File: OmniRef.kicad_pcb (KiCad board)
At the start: 2 copper layers, 79.5 x 50.5 mm, 105 parts, among them J1 4mm Banana Jack Pair, J2 4mm Banana Jack Pair, Q1 PMBT3906, SW1 SW_DPDT_x2, U1 REFERENCE IC, U2 LP2951, U3 REFERENCE IC, U4 AP3015

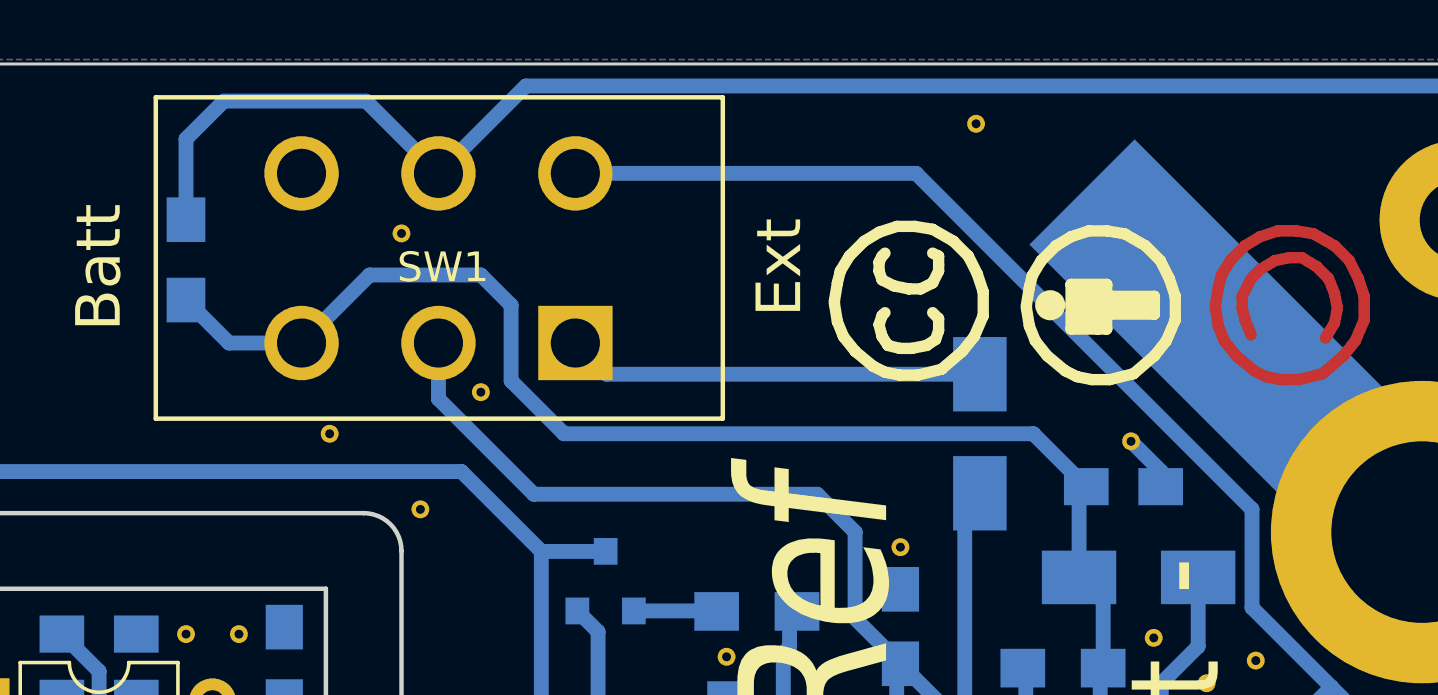
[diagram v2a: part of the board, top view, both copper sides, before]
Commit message: Selected resistors for switching regulator.  Fixed SW1 wiring.
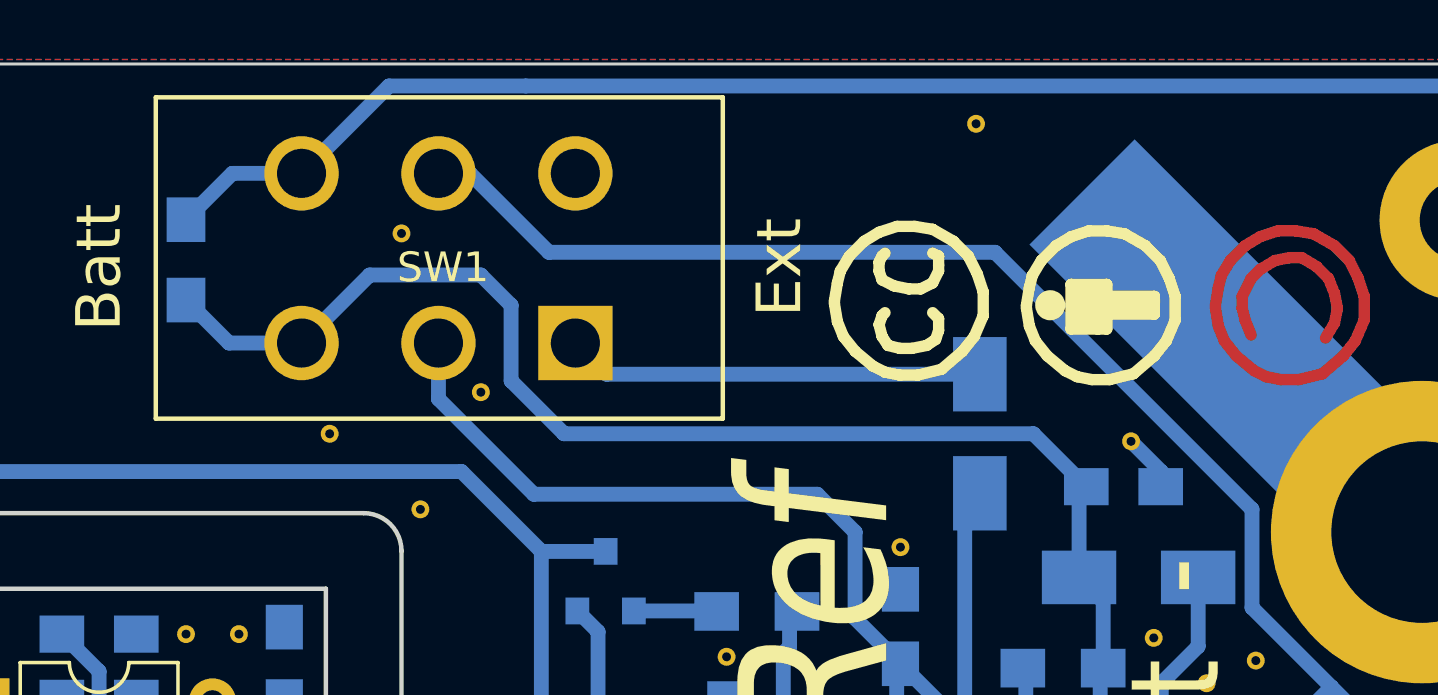
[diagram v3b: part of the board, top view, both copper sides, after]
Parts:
- R12: value R -> 1M
- R13: value R -> 82K
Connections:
- BT1 pad 0: GND -> (no net)
- SW1 pad 4: Net-(C11-Pad1) -> Net-(SW1-Pad4)
- SW1 pad 5: Net-(BT1-Pad1) -> Net-(C11-Pad1)
- SW1 pad 6: (no net) -> Net-(BT1-Pad1)
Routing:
- net Net-(C11-Pad1): track 53.1 -> 57.7 mm
- net Net-(BT1-Pad1): track 140.1 -> 136.5 mm
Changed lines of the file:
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@@
 (kicad_pcb (version 4) (host pcbnew 4.0.5)
   (general
-    (links 152)
+    (links 148)
     (no_connects 0)
-    (area 104.242399 57.785799 184.047601 108.584201)
+    (area 104.344999 57.884999 183.945001 108.485001)
     (thickness 1.6)
     (drawings 38)
-    (tracks 235)
+    (tracks 236)
     (zones 0)
     (modules 105)
-    (nets 26)
+    (nets 27)
   )
   (page A4)
@@
   (net 24 "Net-(C12-Pad2)")
   (net 25 "Net-(D8-Pad2)")
+  (net 26 "Net-(SW1-Pad4)")
   (net_class Default "This is the default net class."
     (clearance 0.2)
@@
     (add_net "Net-(Q1-Pad1)")
     (add_net "Net-(R2-Pad1)")
+    (add_net "Net-(SW1-Pad4)")
     (add_net "Net-(U2-Pad2)")
     (add_net "Net-(U2-Pad6)")
@@
     )
     (pad 0 thru_hole circle (at 8.89 -3.81) (size 2 2) (drill 1.5) (layers *.Cu)
-      (net 2 GND) (zone_connect 2))
+      (zone_connect 2))
     (pad 0 thru_hole circle (at 5.08 -3.81) (size 2 2) (drill 1.5) (layers *.Cu)
-      (net 2 GND) (zone_connect 2))
+      (zone_connect 2))
     (pad 0 thru_hole circle (at 8.89 0) (size 2 2) (drill 1.5) (layers *.Cu)
-      (net 2 GND) (zone_connect 2))
+      (zone_connect 2))
     (pad 2 smd oval (at 0 -3.81) (size 5.08 2.54) (layers B.Cu B.Mask)
       (net 2 GND))
@@
       (net 22 "Net-(BT1-Pad1)"))
     (pad 0 thru_hole circle (at 5.08 0) (size 2 2) (drill 1.5) (layers *.Cu)
-      (net 2 GND) (zone_connect 2))
+      (zone_connect 2))
   )
   (module _NTSFootprints:Via_Tented_0.3mm (layer F.Cu)
@@
       (net 17 BAT+))
     (pad 4 thru_hole circle (at 0 5.7 180) (size 2.5 2.5) (drill 1.65) (layers *.Cu *.Mask)
-      (net 23 "Net-(C11-Pad1)"))
+      (net 26 "Net-(SW1-Pad4)"))
     (pad 5 thru_hole circle (at 4.6 5.7 180) (size 2.5 2.5) (drill 1.65) (layers *.Cu *.Mask)
+      (net 23 "Net-(C11-Pad1)"))
+    (pad 6 thru_hole circle (at 9.2 5.7 180) (size 2.5 2.5) (drill 1.65) (layers *.Cu *.Mask)
       (net 22 "Net-(BT1-Pad1)"))
-    (pad 6 thru_hole circle (at 9.2 5.7 180) (size 2.5 2.5) (drill 1.65) (layers *.Cu *.Mask))
     (model ${KISYS3DMOD}/Buttons_Switches_THT.3dshapes/SW_CuK_JS202011CQN_DPDT_Straight.wrl
       (at (xyz 0 0 0))
@@
       (effects (font (size 1 1) (thickness 0.15)) (justify mirror))
     )
-    (fp_text value R (at 0 -1.75 180) (layer B.Fab)
+    (fp_text value 1M (at 0 -1.75 180) (layer B.Fab)
       (effects (font (size 1 1) (thickness 0.15)) (justify mirror))
     )
@@
       (effects (font (size 1 1) (thickness 0.15)) (justify mirror))
     )
-    (fp_text value R (at 0 -1.75 270) (layer B.Fab)
+    (fp_text value 82K (at 0 -1.75 270) (layer B.Fab)
       (effects (font (size 1 1) (thickness 0.15)) (justify mirror))
     )
@@
   (segment (start 155.913 77.513) (end 155.702 77.724) (width 0.5) (layer B.Cu) (net 14))
   (segment (start 148.336 70.358) (end 164.104 70.358) (width 0.5) (layer B.Cu) (net 17))
-  (segment (start 139.517 67.31) (end 141.803 65.024) (width 0.5) (layer B.Cu) (net 17))
   (segment (start 148.336 70.358) (end 146.558 68.58) (width 0.5) (layer B.Cu) (net 17))
   (segment (start 146.558 68.58) (end 146.558 66.04) (width 0.5) (layer B.Cu) (net 17))
   (segment (start 146.558 66.04) (end 145.542 65.024) (width 0.5) (layer B.Cu) (net 17))
-  (segment (start 145.542 65.024) (end 141.803 65.024) (width 0.5) (layer B.Cu) (net 17))
   (segment (start 164.104 70.358) (end 165.882 72.136) (width 0.5) (layer B.Cu) (net 17))
   (segment (start 165.64 75.184) (end 165.64 72.378) (width 0.5) (layer B.Cu) (net 17))
@@
   (segment (start 166.35 80.264) (end 166.35 78.332) (width 0.5) (layer B.Cu) (net 17))
   (segment (start 166.35 78.332) (end 166.45 78.232) (width 0.5) (layer B.Cu) (net 17))
-  (segment (start 139.517 67.31) (end 137.08 67.31) (width 0.5) (layer B.Cu) (net 17))
   (segment (start 137.08 67.31) (end 135.636 65.866) (width 0.5) (layer B.Cu) (net 17))
+  (segment (start 145.542 65.024) (end 141.803 65.024) (width 0.5) (layer B.Cu) (net 17))
+  (segment (start 139.517 67.31) (end 141.803 65.024) (width 0.5) (layer B.Cu) (net 17))
+  (segment (start 139.517 67.31) (end 137.08 67.31) (width 0.5) (layer B.Cu) (net 17))
   (segment (start 162.306 68.358) (end 149.765 68.358) (width 0.5) (layer B.Cu) (net 18))
   (segment (start 149.765 68.358) (end 148.717 67.31) (width 0.5) (layer B.Cu) (net 18))
@@
   (segment (start 152.94 94.71) (end 153.67 93.98) (width 0.5) (layer B.Cu) (net 21))
   (segment (start 149.32 95.885) (end 152.94 95.885) (width 0.5) (layer B.Cu) (net 21))
-  (segment (start 144.117 67.31) (end 144.117 69.187) (width 0.5) (layer B.Cu) (net 21))
-  (segment (start 144.117 69.187) (end 147.32 72.39) (width 0.5) (layer B.Cu) (net 21))
-  (segment (start 147.32 72.39) (end 156.845 72.39) (width 0.5) (layer B.Cu) (net 21))
-  (segment (start 156.845 72.39) (end 158.115 73.66) (width 0.5) (layer B.Cu) (net 21))
-  (segment (start 158.115 73.66) (end 158.115 76.561) (width 0.5) (layer B.Cu) (net 21))
   (segment (start 158.115 76.561) (end 159.639 78.085) (width 0.5) (layer B.Cu) (net 21))
   (segment (start 159.639 78.085) (end 159.365 78.085) (width 0.5) (layer B.Cu) (net 21))
   (segment (start 159.512 80.485) (end 159.512 78.212) (width 0.5) (layer B.Cu) (net 21))
+  (segment (start 158.115 73.66) (end 158.115 76.561) (width 0.5) (layer B.Cu) (net 21))
+  (segment (start 156.845 72.39) (end 158.115 73.66) (width 0.5) (layer B.Cu) (net 21))
+  (segment (start 144.117 67.31) (end 144.117 69.187) (width 0.5) (layer B.Cu) (net 21))
+  (segment (start 144.117 69.187) (end 147.32 72.39) (width 0.5) (layer B.Cu) (net 21))
+  (segment (start 147.32 72.39) (end 156.845 72.39) (width 0.5) (layer B.Cu) (net 21))
+  (segment (start 147.053 58.674) (end 142.453 58.674) (width 0.5) (layer B.Cu) (net 22))
+  (segment (start 178.816 58.674) (end 147.053 58.674) (width 0.5) (layer B.Cu) (net 22))
+  (segment (start 182.88 62.738) (end 178.816 58.674) (width 0.5) (layer B.Cu) (net 22))
+  (segment (start 179.07 107.696) (end 182.88 103.886) (width 0.5) (layer B.Cu) (net 22))
+  (segment (start 182.88 103.886) (end 182.88 62.738) (width 0.5) (layer B.Cu) (net 22))
+  (segment (start 157.988 107.696) (end 179.07 107.696) (width 0.5) (layer B.Cu) (net 22))
+  (segment (start 142.453 58.674) (end 139.517 61.61) (width 0.5) (layer B.Cu) (net 22))
+  (segment (start 139.517 61.61) (end 137.192 61.61) (width 0.5) (layer B.Cu) (net 22))
+  (segment (start 137.192 61.61) (end 135.636 63.166) (width 0.5) (layer B.Cu) (net 22))
   (segment (start 159.766 103.6) (end 159.766 105.918) (width 0.5) (layer B.Cu) (net 22))
   (segment (start 159.766 105.918) (end 157.988 107.696) (width 0.5) (layer B.Cu) (net 22))
@@
   (segment (start 146.304 105.156) (end 148.844 107.696) (width 0.5) (layer B.Cu) (net 22))
   (segment (start 148.844 107.696) (end 157.988 107.696) (width 0.5) (layer B.Cu) (net 22))
-  (segment (start 157.988 107.696) (end 179.07 107.696) (width 0.5) (layer B.Cu) (net 22))
-  (segment (start 179.07 107.696) (end 182.88 103.886) (width 0.5) (layer B.Cu) (net 22))
-  (segment (start 182.88 103.886) (end 182.88 62.738) (width 0.5) (layer B.Cu) (net 22))
-  (segment (start 182.88 62.738) (end 178.816 58.674) (width 0.5) (layer B.Cu) (net 22))
-  (segment (start 178.816 58.674) (end 147.053 58.674) (width 0.5) (layer B.Cu) (net 22))
-  (segment (start 147.053 58.674) (end 144.117 61.61) (width 0.5) (layer B.Cu) (net 22))
-  (segment (start 135.636 63.166) (end 135.636 60.452) (width 0.5) (layer B.Cu) (net 22))
-  (segment (start 141.689 59.182) (end 144.117 61.61) (width 0.5) (layer B.Cu) (net 22))
-  (segment (start 136.906 59.182) (end 141.689 59.182) (width 0.5) (layer B.Cu) (net 22))
-  (segment (start 135.636 60.452) (end 136.906 59.182) (width 0.5) (layer B.Cu) (net 22))
+  (segment (start 144.117 61.61) (end 145.176 61.61) (width 0.5) (layer B.Cu) (net 23))
+  (segment (start 145.176 61.61) (end 147.828 64.262) (width 0.5) (layer B.Cu) (net 23))
+  (segment (start 147.828 64.262) (end 162.814 64.262) (width 0.5) (layer B.Cu) (net 23))
+  (segment (start 162.814 64.262) (end 171.45 72.898) (width 0.5) (layer B.Cu) (net 23))
   (segment (start 170.514 83.886) (end 170.514 85.786) (width 0.5) (layer B.Cu) (net 23))
   (segment (start 172.446 80.264) (end 172.446 81.954) (width 0.5) (layer B.Cu) (net 23))
@@
   (segment (start 172.72 80.264) (end 174.117 78.867) (width 0.5) (layer B.Cu) (net 23))
   (segment (start 174.752 79.502) (end 179.324 79.502) (width 0.5) (layer B.Cu) (net 23))
-  (segment (start 171.45 76.2) (end 174.117 78.867) (width 0.5) (layer B.Cu) (net 23))
   (segment (start 174.117 78.867) (end 174.752 79.502) (width 0.5) (layer B.Cu) (net 23))
-  (segment (start 171.45 72.898) (end 171.45 76.2) (width 0.5) (layer B.Cu) (net 23))
-  (segment (start 160.162 61.61) (end 171.45 72.898) (width 0.5) (layer B.Cu) (net 23))
-  (segment (start 148.717 61.61) (end 160.162 61.61) (width 0.5) (layer B.Cu) (net 23))
   (segment (start 179.324 79.502) (end 181.083 81.261) (width 0.5) (layer B.Cu) (net 23))
   (segment (start 181.083 81.261) (end 181.083 83.312) (width 0.5) (layer B.Cu) (net 23))
+  (segment (start 171.45 76.2) (end 174.117 78.867) (width 0.5) (layer B.Cu) (net 23))
+  (segment (start 171.45 72.898) (end 171.45 76.2) (width 0.5) (layer B.Cu) (net 23))
   (segment (start 163.85 80.264) (end 163.85 78.332) (width 0.5) (layer B.Cu) (net 24))
   (segment (start 163.85 78.332) (end 163.75 78.232) (width 0.5) (layer B.Cu) (net 24))

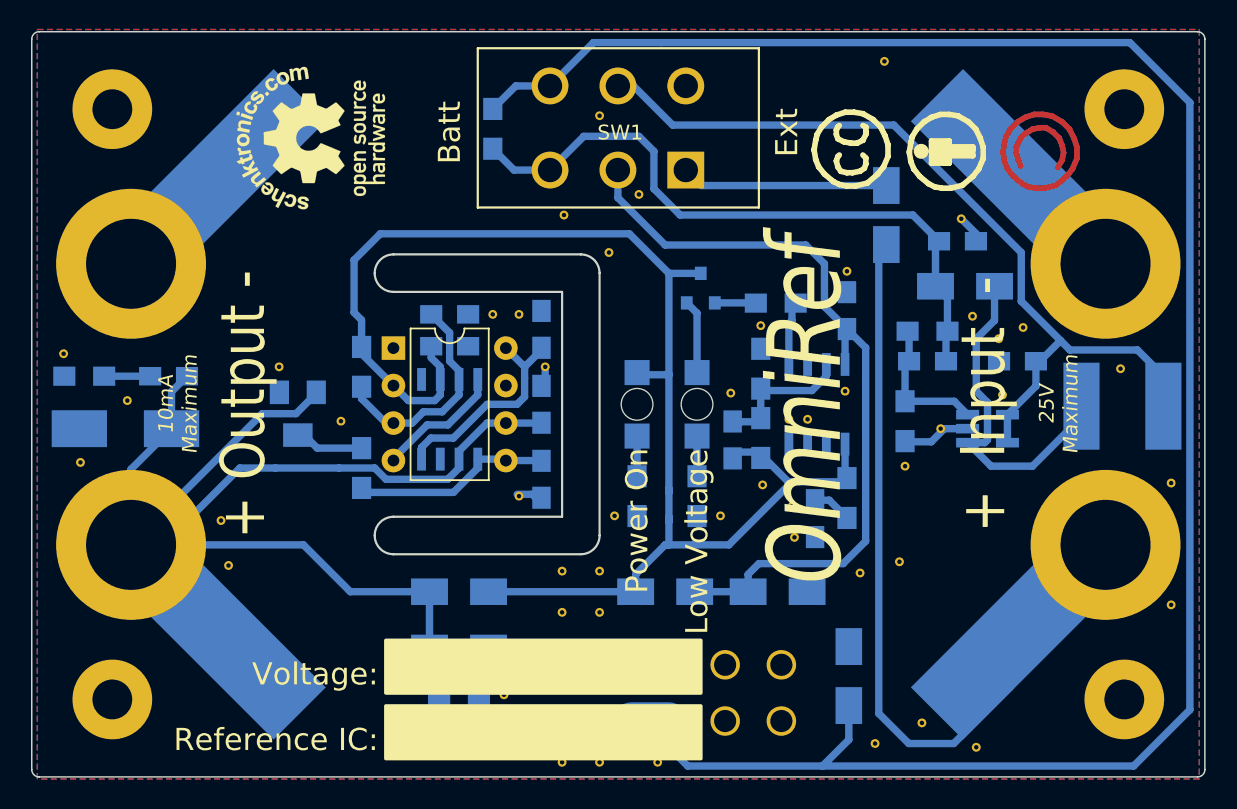
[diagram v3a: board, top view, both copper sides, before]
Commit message: Fixed a number of issues discovered during prototyping.  Re-arranged logos a bit.
Moved RV1 between output jacks to clear battery.
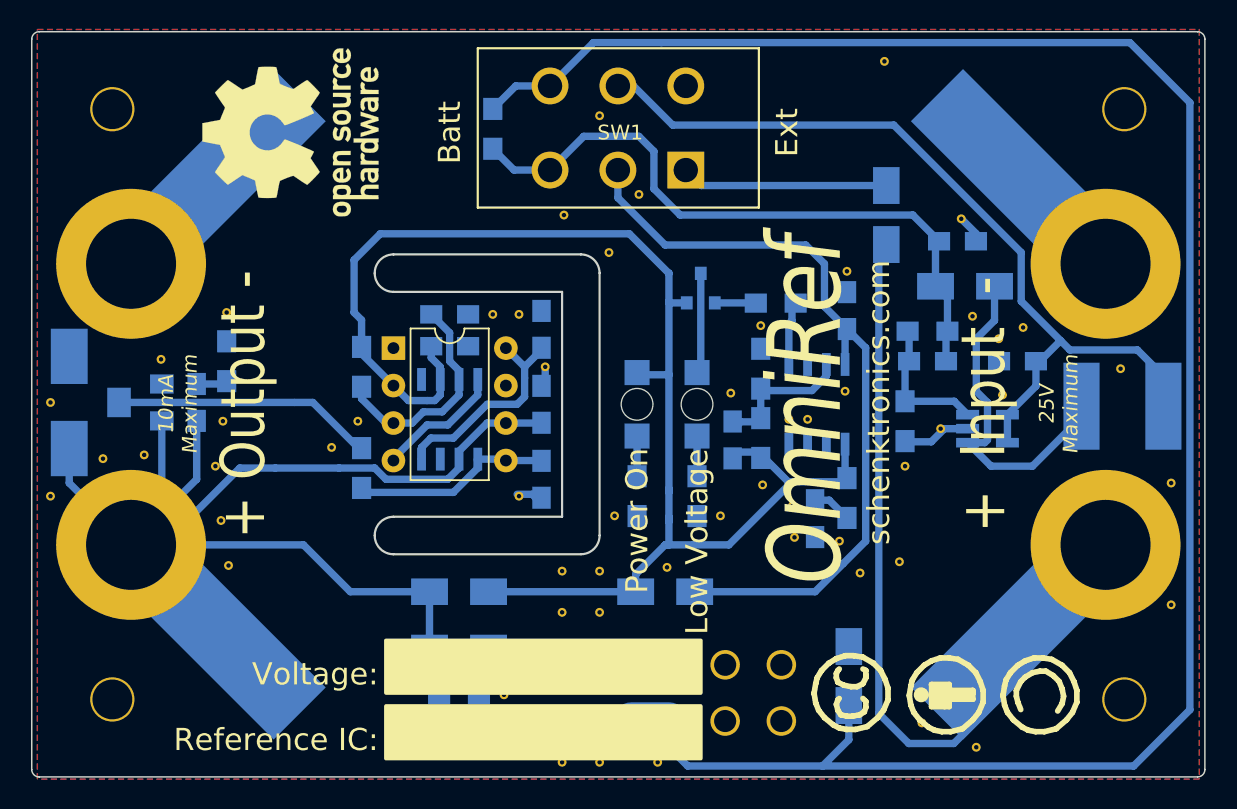
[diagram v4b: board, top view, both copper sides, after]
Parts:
- removed D4: SMA, Diodes_SMD:D_SMA
- removed G***: LOGO, _NTSFootprints:schenktronics.com_OSHW_Logo_11x11mm
- removed the REF** at (161.5, 106.2)
- added REF**: 1pin, _NTSFootprints:Via_Tented_0.3mm, F.Cu at (113.2, 80.1)
- added REF**: 1pin, _NTSFootprints:Via_Tented_0.3mm, F.Cu at (109.2, 86.9)
- added REF**: 1pin, _NTSFootprints:Via_Tented_0.3mm, F.Cu at (112.0, 86.6)
- added REF**: 1pin, _NTSFootprints:Via_Tented_0.3mm, F.Cu at (105.7, 89.4)
- added REF**: 1pin, _NTSFootprints:Via_Tented_0.3mm, F.Cu at (117.3, 84.3)
- added REF**: 1pin, _NTSFootprints:Via_Tented_0.3mm, F.Cu at (147.4, 94.2)
- added REF**: 1pin, _NTSFootprints:Via_Tented_0.3mm, F.Cu at (159.1, 92.5)
- added REF***: OSHW-Logo_11.4x12mm_SilkScreen, Symbols:OSHW-Logo_11.4x12mm_SilkScreen, F.Cu at (121.9, 64.8)
- R1: value 2.4K -> 10K
- R10, R7: value 1K -> 3.6K
- R3: value 270 -> 100K
- REF**: footprint Symbols:Symbol_CC-ShareAlike_CopperTop_Small -> _NTSFootprints:Symbol_CC-ShareAlike_SilkTop_Small
- moved REF** 36.8 mm to (160.0, 102.9)
- moved REF** 36.8 mm to (166.4, 102.9)
- moved REF** 36.8 mm to (172.7, 102.9)
- moved RV1 10.7 mm to (111.8, 83.1), turned to 90 degrees
- moved R6 9.71 mm to (117.6, 80.3), turned to 90 degrees
- moved REF** 9.15 mm to (116.8, 87.4)
- moved REF** 9.00 mm to (117.6, 77.0)
- moved REF** 6.52 mm to (124.7, 86.1)
- moved C9 4.20 mm to (106.9, 83.1), turned to 90 degrees
- moved REF** 3.42 mm to (105.7, 83.1)
- moved C7 2.61 mm to (115.6, 83.1), turned to 90 degrees
- moved REF** 1.14 mm to (126.5, 84.3)
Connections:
- BT1 pad 0: (no net) -> GND
- Q1 pad 2: Net-(D5-Pad2) -> V+
- Q1 pad 3: V+ -> Net-(D5-Pad2)
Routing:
- net Net-(R2-Pad1): track 5.36 -> 17.9 mm
- net Net-(D5-Pad2): track 5.16 -> 6.83 mm
- net Net-(C7-Pad2): track 3.12 -> 2.11 mm
- net Net-(C7-Pad1): track 103.4 -> 104.3 mm
- net V+: track 99.1 -> 98.3 mm
- net Net-(C2-Pad1): track 53.9 -> 53.2 mm
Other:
- board text added: "schenktronics.com"

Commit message: Adjusted OSHW logo.
Made PDF's of the schematic and board.
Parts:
- removed REF***: OSHW-Logo_11.4x12mm_SilkScreen, Symbols:OSHW-Logo_11.4x12mm_SilkScreen
- added G***: OSHW_LOGO_EEVBlog, _NTSFootprints:OSHW_LOGO_EEVBlog, F.Cu at (122.6, 66.0)
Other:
- board text added: "OmniRef v1.0"
